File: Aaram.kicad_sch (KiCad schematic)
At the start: 51 parts, among them J1 Conn_01x03, J2 Conn_01x02, J3 AC_OUT, J4 SWITCH_IN, J5 5V_OUT, J6 PSU_AC_IN, J8 SPARE_PINS, K1 10A cube relay, K2 10A cube relay, K3 10A cube relay, Q1 BT136-600, Q2 2N2222A, Q3 2N2222A, Q4 2N2222A, U1 ESP32-DevKitC, U2 TLP281-4GB_F_

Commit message: Added 5v connection to relays
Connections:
- net +5V: now also D1.1 (K), D2.1 (K), D3.1 (K), K1.5, K2.5, K3.5
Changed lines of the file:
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@@
 	)
 	(junction
+		(at 236.22 121.92)
+		(diameter 0)
+		(color 0 0 0 0)
+	)
+	(junction
 		(at 184.15 95.25)
 		(diameter 0)
@@
 	)
 	(junction
+		(at 251.46 24.13)
+		(diameter 0)
+		(color 0 0 0 0)
+	)
+	(junction
 		(at 62.23 55.88)
 		(diameter 0)
@@
 	)
 	(junction
+		(at 240.03 71.12)
+		(diameter 0)
+		(color 0 0 0 0)
+	)
+	(junction
 		(at 72.39 25.4)
 		(diameter 0)
@@
 	)
 	(symbol
+		(lib_id "power:+5V")
+		(at 251.46 24.13 0)
+		(unit 1)
+		(exclude_from_sim no)
+		(in_bom yes)
+		(on_board yes)
+		(dnp no)
+		(property "Reference" "#PWR04"
+			(at 251.46 27.94 0)
+			(effects
+				(font
+					(size 1.27 1.27)
+				)
+				(hide yes)
+			)
+		)
+		(property "Value" "+5V"
+			(at 251.4601 20.32 90)
+			(effects
+				(font
+					(size 1.27 1.27)
+				)
+				(justify left)
+			)
+		)
+		(property "Footprint" ""
+			(at 251.46 24.13 0)
+			(effects
+				(font
+					(size 1.27 1.27)
+				)
+				(hide yes)
+			)
+		)
+		(property "Datasheet" ""
+			(at 251.46 24.13 0)
+			(effects
+				(font
+					(size 1.27 1.27)
+				)
+				(hide yes)
+			)
+		)
+		(property "Description" "Power symbol creates a global label with name \"+5V\""
+			(at 251.46 24.13 0)
+			(effects
+				(font
+					(size 1.27 1.27)
+				)
+				(hide yes)
+			)
+		)
+		(pin "1"
+		)
+		(instances
+			(project "Aaram"
+				(path "/29654a86-74fd-4059-9f21-82ff906cc333"
+					(reference "#PWR04")
+					(unit 1)
+				)
+			)
+		)
+	)
+	(symbol
 		(lib_id "PCM_Resistor_AKL:R_1206")
 		(at 62.23 44.45 180)
@@
 	)
 	(symbol
+		(lib_id "power:+5V")
+		(at 236.22 121.92 90)
+		(unit 1)
+		(exclude_from_sim no)
+		(in_bom yes)
+		(on_board yes)
+		(dnp no)
+		(property "Reference" "#PWR06"
+			(at 240.03 121.92 0)
+			(effects
+				(font
+					(size 1.27 1.27)
+				)
+				(hide yes)
+			)
+		)
+		(property "Value" "+5V"
+			(at 232.41 121.9199 90)
+			(effects
+				(font
+					(size 1.27 1.27)
+				)
+				(justify left)
+			)
+		)
+		(property "Footprint" ""
+			(at 236.22 121.92 0)
+			(effects
+				(font
+					(size 1.27 1.27)
+				)
+				(hide yes)
+			)
+		)
+		(property "Datasheet" ""
+			(at 236.22 121.92 0)
+			(effects
+				(font
+					(size 1.27 1.27)
+				)
+				(hide yes)
+			)
+		)
+		(property "Description" "Power symbol creates a global label with name \"+5V\""
+			(at 236.22 121.92 0)
+			(effects
+				(font
+					(size 1.27 1.27)
+				)
+				(hide yes)
+			)
+		)
+		(pin "1"
+		)
+		(instances
+			(project "Aaram"
+				(path "/29654a86-74fd-4059-9f21-82ff906cc333"
+					(reference "#PWR06")
+					(unit 1)
+				)
+			)
+		)
+	)
+	(symbol
 		(lib_id "PCM_Resistor_AKL:R_1206")
 		(at 165.1 127 0)
@@
 					(unit 1)
 				)
+			)
+		)
+	)
+	(symbol
+		(lib_id "power:+5V")
+		(at 240.03 71.12 90)
+		(unit 1)
+		(exclude_from_sim no)
+		(in_bom yes)
+		(on_board yes)
+		(dnp no)
+		(property "Reference" "#PWR05"
+			(at 243.84 71.12 0)
+			(effects
+				(font
+					(size 1.27 1.27)
+				)
+				(hide yes)
+			)
+		)
+		(property "Value" "+5V"
+			(at 236.22 71.1199 90)
+			(effects
+				(font
+					(size 1.27 1.27)
+				)
+				(justify left)
+			)
+		)
+		(property "Footprint" ""
+			(at 240.03 71.12 0)
+			(effects
+				(font
+					(size 1.27 1.27)
+				)
+				(hide yes)
+			)
+		)
+		(property "Datasheet" ""
+			(at 240.03 71.12 0)
+			(effects
+				(font
+					(size 1.27 1.27)
+				)
+				(hide yes)
+			)
+		)
+		(property "Description" "Power symbol creates a global label with name \"+5V\""
+			(at 240.03 71.12 0)
+			(effects
+				(font
+					(size 1.27 1.27)
+				)
+				(hide yes)
+			)
+		)
+		(pin "1"
+		)
+		(instances
+			(project "Aaram"
+				(path "/29654a86-74fd-4059-9f21-82ff906cc333"
+					(reference "#PWR05")
+					(unit 1)
+				)

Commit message: Updated Silkscreen and connections
Moved the fan control from GPIO4 to GPIO 13, made changes to the silkscreen and redid some of the tracks for better layout.
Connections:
- net SP1: no longer U1.15 (MTCK/GPIO13/ADC2_CH4)
- net T1_Pin: now also U1.15 (MTCK/GPIO13/ADC2_CH4); no longer U1.26 (ADC2_CH0/GPIO4)
- no-connect marks 18 -> 19
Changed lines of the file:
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@@
+	)
+	(no_connect
+		(at 106.68 97.79)
 	)
 	(no_connect
@@
 		)
 	)
+	(global_label "T1_Pin"
+		(shape input)
+		(at 40.64 100.33 180)
+		(fields_autoplaced yes)
+		(effects
+			(font
+				(size 1.27 1.27)
+			)
+			(justify right)
+		)
+		(property "Intersheetrefs" "${INTERSHEET_REFS}"
+			(at 31.4863 100.33 0)
+			(effects
+				(font
+					(size 1.27 1.27)
+				)
+				(justify right)
+				(hide yes)
+			)
+		)
+	)
 	(global_label "S1"
 		(shape input)
@@
 		)
 	)
-	(global_label "SP1"
-		(shape input)
-		(at 40.64 100.33 180)
-		(fields_autoplaced yes)
-		(effects
-			(font
-				(size 1.27 1.27)
-			)
-			(justify right)
-		)
-		(property "Intersheetrefs" "${INTERSHEET_REFS}"
-			(at 33.9658 100.33 0)
-			(effects
-				(font
-					(size 1.27 1.27)
-				)
-				(justify right)
-				(hide yes)
-			)
-		)
-	)
 	(global_label "S4"
 		(shape input)
@@
 				(hide yes)
 			)
-		)
-	)
-	(global_label "T1_Pin"
-		(shape input)
-		(at 106.68 97.79 0)
-		(fields_autoplaced yes)
-		(effects
-			(font
-				(size 1.27 1.27)
-			)
-			(justify left)
-		)
-		(property "Intersheetrefs" "${INTERSHEET_REFS}"
-			(at 115.8337 97.79 0)
-			(effects
-				(font
-					(size 1.27 1.27)
-				)
-				(justify left)
-				(hide yes)
-			)

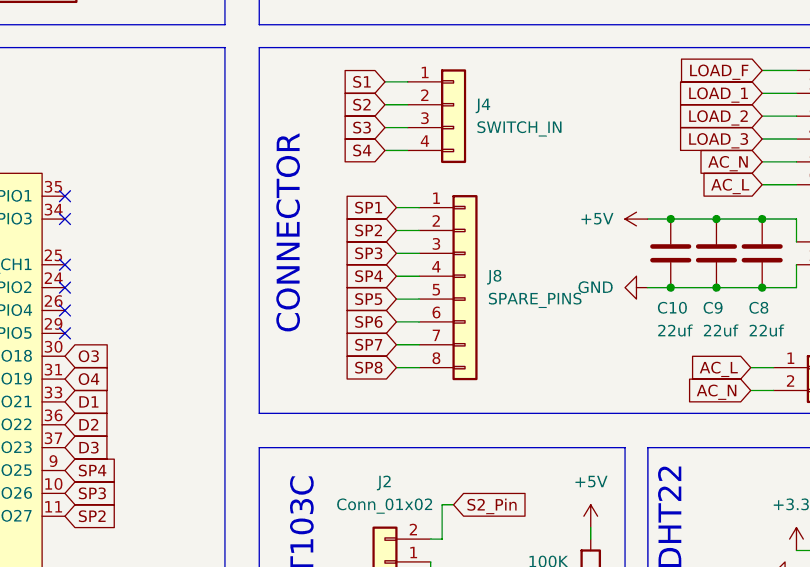
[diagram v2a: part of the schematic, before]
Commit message: Component update
Changed most of the components to use SMD form factor, updated clearance between components in the AC zone and updated the tracks.
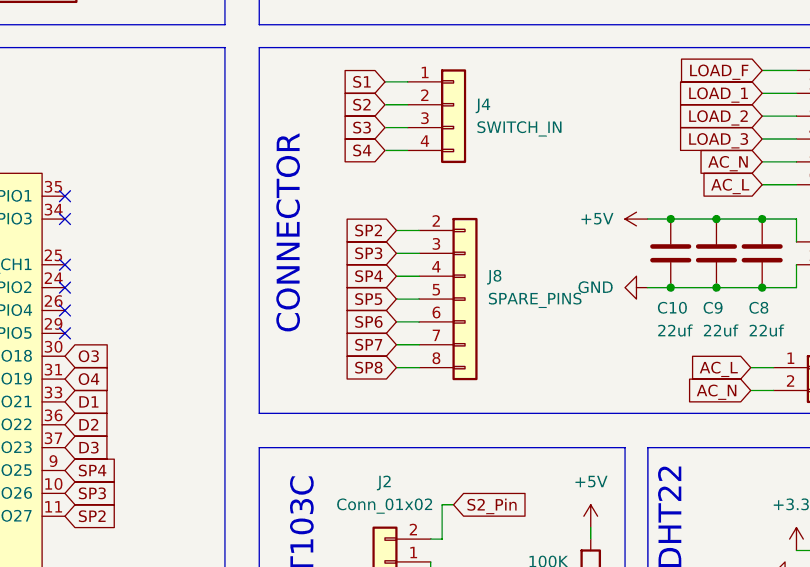
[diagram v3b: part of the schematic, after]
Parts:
- C10, C8, C9: footprint PCM_Capacitor_SMD_AKL:C_1206_3216Metric -> PCM_Capacitor_SMD_Handsoldering_AKL:C_1206_3216Metric_Pad1.42x1.75mm
- D1, D2, D3, D4, D5, D6, D7: footprint Diode_THT:D_DO-41_SOD81_P10.16mm_Horizontal -> Diode_SMD:D_SMA_Handsoldering
- Q2, Q3, Q4: footprint PCM_Package_TO_SOT_THT_AKL:TO-18-3_EBC -> PCM_Package_TO_SOT_SMD_AKL:SOT-23_BigPads
- R1, R10, R11, R12, R13, R14, R15, R16, R17, R2, R3, R4, R5, R6, R7, R8, R9: footprint PCM_Resistor_SMD_AKL:R_1206_3216Metric -> PCM_Capacitor_SMD_Handsoldering_AKL:C_1206_3216Metric_Pad1.42x1.75mm
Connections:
- removed net SP1: J8.1 (Pin_1)
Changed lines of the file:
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@@
 	(wire
 		(pts
-			(xy 143.51 86.36) (xy 146.05 86.36)
-		)
-		(stroke
-			(width 0)
-			(type default)
-		)
-	)
-	(wire
-		(pts
 			(xy 142.24 72.39) (xy 144.78 72.39)
 		)
@@
 		)
 	)
-	(global_label "SP1"
-		(shape input)
-		(at 143.51 86.36 180)
-		(fields_autoplaced yes)
-		(effects
-			(font
-				(size 1.27 1.27)
-			)
-			(justify right)
-		)
-		(property "Intersheetrefs" "${INTERSHEET_REFS}"
-			(at 136.8358 86.36 0)
-			(effects
-				(font
-					(size 1.27 1.27)
-				)
-				(justify right)
-				(hide yes)
-			)
-		)
-	)
 	(global_label "LOAD_F"
 		(shape input)
@@
 			)
 		)
-		(property "Footprint" "PCM_Package_TO_SOT_THT_AKL:TO-18-3_EBC"
+		(property "Footprint" "PCM_Package_TO_SOT_SMD_AKL:SOT-23_BigPads"
 			(at 254 91.44 0)
 			(effects
@@
 			)
 		)
-		(property "Footprint" "Diode_THT:D_DO-41_SOD81_P10.16mm_Horizontal"
+		(property "Footprint" "Diode_SMD:D_SMA_Handsoldering"
 			(at 68.58 20.955 0)
 			(effects
@@
 			)
 		)
-		(property "Footprint" "PCM_Resistor_SMD_AKL:R_1206_3216Metric"
+		(property "Footprint" "PCM_Capacitor_SMD_Handsoldering_AKL:C_1206_3216Metric_Pad1.42x1.75mm"
 			(at 62.23 33.02 0)
 			(effects
@@
 			)
 		)
-		(property "Footprint" "PCM_Resistor_SMD_AKL:R_1206_3216Metric"
+		(property "Footprint" "PCM_Capacitor_SMD_Handsoldering_AKL:C_1206_3216Metric_Pad1.42x1.75mm"
 			(at 226.06 46.99 0)
 			(effects
@@
 			)
 		)
-		(property "Footprint" "PCM_Resistor_SMD_AKL:R_1206_3216Metric"
+		(property "Footprint" "PCM_Capacitor_SMD_Handsoldering_AKL:C_1206_3216Metric_Pad1.42x1.75mm"
 			(at 190.5 24.13 0)
 			(effects
@@
 			)
 		)
-		(property "Footprint" "PCM_Resistor_SMD_AKL:R_1206_3216Metric"
+		(property "Footprint" "PCM_Capacitor_SMD_Handsoldering_AKL:C_1206_3216Metric_Pad1.42x1.75mm"
 			(at 33.02 40.64 0)
 			(effects
@@
 			)
 		)
-		(property "Footprint" "PCM_Capacitor_SMD_AKL:C_1206_3216Metric"
+		(property "Footprint" "PCM_Capacitor_SMD_Handsoldering_AKL:C_1206_3216Metric_Pad1.42x1.75mm"
 			(at 174.9552 95.25 0)
 			(effects
@@
 			)
 		)
-		(property "Footprint" "PCM_Resistor_SMD_AKL:R_1206_3216Metric"
+		(property "Footprint" "PCM_Capacitor_SMD_Handsoldering_AKL:C_1206_3216Metric_Pad1.42x1.75mm"
 			(at 33.02 10.16 0)
 			(effects
@@
 			)
 		)
-		(property "Footprint" "PCM_Package_TO_SOT_THT_AKL:TO-18-3_EBC"
+		(property "Footprint" "PCM_Package_TO_SOT_SMD_AKL:SOT-23_BigPads"
 			(at 254 44.45 0)
 			(effects
@@
 			)
 		)
-		(property "Footprint" "Diode_THT:D_DO-41_SOD81_P10.16mm_Horizontal"
+		(property "Footprint" "Diode_SMD:D_SMA_Handsoldering"
 			(at 68.58 43.815 0)
 			(effects
@@
 			)
 		)
-		(property "Footprint" "PCM_Resistor_SMD_AKL:R_1206_3216Metric"
+		(property "Footprint" "PCM_Capacitor_SMD_Handsoldering_AKL:C_1206_3216Metric_Pad1.42x1.75mm"
 			(at 165.1 148.59 0)
 			(effects
@@
 			)
 		)
-		(property "Footprint" "PCM_Capacitor_SMD_AKL:C_1206_3216Metric"
+		(property "Footprint" "PCM_Capacitor_SMD_Handsoldering_AKL:C_1206_3216Metric_Pad1.42x1.75mm"
 			(at 180.0352 95.25 0)
 			(effects
@@
 			)
 		)
-		(property "Footprint" "PCM_Resistor_SMD_AKL:R_1206_3216Metric"
+		(property "Footprint" "PCM_Capacitor_SMD_Handsoldering_AKL:C_1206_3216Metric_Pad1.42x1.75mm"
 			(at 62.23 10.16 0)
 			(effects
@@
 			)
 		)
-		(property "Footprint" "PCM_Resistor_SMD_AKL:R_1206_3216Metric"
+		(property "Footprint" "PCM_Capacitor_SMD_Handsoldering_AKL:C_1206_3216Metric_Pad1.42x1.75mm"
 			(at 166.37 36.83 0)
 			(effects
@@
 			)
 		)
-		(property "Footprint" "PCM_Resistor_SMD_AKL:R_1206_3216Metric"
+		(property "Footprint" "PCM_Capacitor_SMD_Handsoldering_AKL:C_1206_3216Metric_Pad1.42x1.75mm"
 			(at 62.23 17.78 0)
 			(effects
@@
 			)
 		)
-		(property "Footprint" "Diode_THT:D_DO-41_SOD81_P10.16mm_Horizontal"
+		(property "Footprint" "Diode_SMD:D_SMA_Handsoldering"
 			(at 235.585 31.75 0)
 			(effects
@@
 			)
 		)
-		(property "Footprint" "PCM_Resistor_SMD_AKL:R_1206_3216Metric"
+		(property "Footprint" "PCM_Capacitor_SMD_Handsoldering_AKL:C_1206_3216Metric_Pad1.42x1.75mm"
 			(at 154.94 36.83 0)
 			(effects
@@
 			)
 		)
-		(property "Footprint" "Diode_THT:D_DO-41_SOD81_P10.16mm_Horizontal"
+		(property "Footprint" "Diode_SMD:D_SMA_Handsoldering"
 			(at 231.775 129.54 0)
 			(effects
@@
 			)
 		)
-		(property "Footprint" "PCM_Resistor_SMD_AKL:R_1206_3216Metric"
+		(property "Footprint" "PCM_Capacitor_SMD_Handsoldering_AKL:C_1206_3216Metric_Pad1.42x1.75mm"
 			(at 33.02 33.02 0)
 			(effects
@@
 			)
 		)
-		(property "Footprint" "Diode_THT:D_DO-41_SOD81_P10.16mm_Horizontal"
+		(property "Footprint" "Diode_SMD:D_SMA_Handsoldering"
 			(at 39.37 43.815 0)
 			(effects
@@
 			)
 		)
-		(property "Footprint" "PCM_Package_TO_SOT_THT_AKL:TO-18-3_EBC"
+		(property "Footprint" "PCM_Package_TO_SOT_SMD_AKL:SOT-23_BigPads"
 			(at 250.19 142.24 0)
 			(effects
@@
 			)
 		)
-		(property "Footprint" "PCM_Resistor_SMD_AKL:R_1206_3216Metric"
+		(property "Footprint" "PCM_Capacitor_SMD_Handsoldering_AKL:C_1206_3216Metric_Pad1.42x1.75mm"
 			(at 62.23 40.64 0)
 			(effects
@@
 			)
 		)
-		(property "Footprint" "PCM_Resistor_SMD_AKL:R_1206_3216Metric"
+		(property "Footprint" "PCM_Capacitor_SMD_Handsoldering_AKL:C_1206_3216Metric_Pad1.42x1.75mm"
 			(at 222.25 144.78 0)
 			(effects
@@
 			)
 		)
-		(property "Footprint" "PCM_Resistor_SMD_AKL:R_1206_3216Metric"
+		(property "Footprint" "PCM_Capacitor_SMD_Handsoldering_AKL:C_1206_3216Metric_Pad1.42x1.75mm"
 			(at 165.1 138.43 0)
 			(effects
@@
 			)
 		)
-		(property "Footprint" "Diode_THT:D_DO-41_SOD81_P10.16mm_Horizontal"
+		(property "Footprint" "Diode_SMD:D_SMA_Handsoldering"
 			(at 39.37 20.955 0)
 			(effects
@@
 			)
 		)
-		(property "Footprint" "PCM_Resistor_SMD_AKL:R_1206_3216Metric"
+		(property "Footprint" "PCM_Capacitor_SMD_Handsoldering_AKL:C_1206_3216Metric_Pad1.42x1.75mm"
 			(at 157.48 36.83 0)
 			(effects
@@
 		(pin "6"
 		)
-		(pin "1"
-		)
 		(instances
 			(project ""
@@
 			)
 		)
-		(property "Footprint" "PCM_Capacitor_SMD_AKL:C_1206_3216Metric"
+		(property "Footprint" "PCM_Capacitor_SMD_Handsoldering_AKL:C_1206_3216Metric_Pad1.42x1.75mm"
 			(at 185.1152 95.25 0)
 			(effects
@@
 			)
 		)
-		(property "Footprint" "PCM_Resistor_SMD_AKL:R_1206_3216Metric"
+		(property "Footprint" "PCM_Capacitor_SMD_Handsoldering_AKL:C_1206_3216Metric_Pad1.42x1.75mm"
 			(at 226.06 93.98 0)
 			(effects
@@
 			)
 		)
-		(property "Footprint" "Diode_THT:D_DO-41_SOD81_P10.16mm_Horizontal"
+		(property "Footprint" "Diode_SMD:D_SMA_Handsoldering"
 			(at 235.585 78.74 0)
 			(effects
@@
 			)
 		)
-		(property "Footprint" "PCM_Resistor_SMD_AKL:R_1206_3216Metric"
+		(property "Footprint" "PCM_Capacitor_SMD_Handsoldering_AKL:C_1206_3216Metric_Pad1.42x1.75mm"
 			(at 33.02 17.78 0)
 			(effects

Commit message: Updated mostly everything
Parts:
- removed C10, C8, C9: 22uf, PCM_Capacitor_SMD_Handsoldering_AKL:C_1206_3216Metric_Pad1.42x1.75mm, symbol PCM_Capacitor_AKL:C_1206
- removed C3, C5, C6, C7: CP_Axial_L10.0mm_D4.5mm_P15.00mm, Xicor_Custom stuff:Axial_Capacitor_P10mm_W4.5mm, symbol PCM_Capacitor_AKL:CP_Axial_L10.0mm_D4.5mm_P15.00mm
- removed D4, D5, D6, D7: 1N4007, Diode_SMD:D_SMA_Handsoldering, symbol Diode:1N4007
- removed J8: SPARE_PINS, Connector_PinHeader_2.54mm:PinHeader_1x08_P2.54mm_Vertical, symbol Connector_Generic:Conn_01x08
- removed R11, R13: 10K, PCM_Capacitor_SMD_Handsoldering_AKL:C_1206_3216Metric_Pad1.42x1.75mm, symbol PCM_Resistor_AKL:R_1206
- removed R16: 1M, PCM_Capacitor_SMD_Handsoldering_AKL:C_1206_3216Metric_Pad1.42x1.75mm, symbol PCM_Resistor_AKL:R_1206
- removed U1: ESP32-DevKitC, Xicor_Custom stuff:ESP32_38Pin, symbol PCM_Espressif:ESP32-DevKitC
- removed U2: TLP281-4GB_F_, Xicor_Custom stuff:SOIC127P700X210-16N, symbol TLP281-4GB_F_:TLP281-4GB_F_
- added C11, C12, C6, C7: 10uf, PCM_Capacitor_SMD_Handsoldering_AKL:C_1206_3216Metric_Pad1.42x1.75mm, symbol PCM_Capacitor_AKL:C_Generic
- added C16: 1uf, PCM_Capacitor_SMD_Handsoldering_AKL:C_1206_3216Metric_Pad1.42x1.75mm, symbol PCM_Capacitor_AKL:C_Generic
- added C18, C19: 0.1uf, PCM_Capacitor_SMD_Handsoldering_AKL:C_1206_3216Metric_Pad1.42x1.75mm, symbol PCM_Capacitor_AKL:C_1206
- added D10, D11, D8, D9: MB6S, PCM_Diode_SMD_AKL:Diode_Bridge_MBS, symbol PCM_Diode_Bridge_AKL:MB6S
- added F1: Fuse, Xicor_Custom stuff:BLX-A, symbol PCM_Device_AKL:Fuse
- added J10, J11, J12, J13: Conn_01x03_Socket, Connector_JST:JST_SH_BM03B-SRSS-TB_1x03-1MP_P1.00mm_Vertical, symbol Connector_Generic:Conn_01x03
- added J7: Conn_01x05, Connector_PinHeader_2.54mm:PinHeader_1x05_P2.54mm_Vertical, symbol Connector_Generic:Conn_01x05
- added J8: USB_C_Receptacle_USB2.0_16P, Connector_USB:USB_C_Receptacle_GCT_USB4105-xx-A_16P_TopMnt_Horizontal, symbol Connector:USB_C_Receptacle_USB2.0_16P
- added J9: Conn_01x02, Connector_PinSocket_2.54mm:PinSocket_1x02_P2.54mm_Vertical, symbol Connector_Generic:Conn_01x02
- added R19, R23: 100K, PCM_Resistor_SMD_AKL:R_1206_3216Metric_Pad1.42x1.75mm_HandSolder, symbol PCM_Resistor_AKL:R_1206
- added R20, R25, R26, R27: 10K, PCM_Resistor_SMD_AKL:R_1206_3216Metric_Pad1.42x1.75mm_HandSolder, symbol PCM_Resistor_AKL:R_1206
- added R21, R22: 10k, PCM_Resistor_SMD_AKL:R_1206_3216Metric_Pad1.42x1.75mm_HandSolder, symbol PCM_Resistor_AKL:R_1206
- added RV1, RV2, RV3, RV4: Varistor, Xicor_Custom stuff:Varistor_10D431K, symbol Device:Varistor
- added SW1, SW4: SW_Push, Xicor_Custom stuff:Tactile switch 6x3, symbol Switch:SW_Push
- added SW2: SW_Push, Xicor_Custom stuff:SMD Tactile switch, symbol Switch:SW_Push
- added U1: ESP32-C6-MINI-1/U, PCM_Espressif:ESP32-C6-MINI-1, symbol PCM_Espressif:ESP32-C6-MINI-1/U
- added U2: AZ1117D-3.3TRE1, PCM_Package_TO_SOT_SMD_AKL:TO-252-2, symbol PCM_Voltage_Regulator_AKL:AZ1117D-3.3TRE1
- added U3: ~, Xicor_Custom stuff:Mini_Boost, symbol Xicor_Custom:Mini_Boost
- added U4: ~, Xicor_Custom stuff:TP4056-18650, symbol Xicor_Custom:TP4056-18650
- added U5: TLP281-4GB_F_, Xicor_Custom stuff:SOP127P780X200-16N, symbol TLP281-4GB_F_:TLP281-4GB_F_
- C1: symbol PCM_Capacitor_AKL:CP_Axial_L10.0mm_D4.5mm_P15.00mm -> PCM_Capacitor_AKL:C_3640
- C2: footprint Xicor_Custom stuff:Film_Cap_13x13mm_P5.00mm -> PCM_Capacitor_SMD_Handsoldering_AKL:C_1206_3216Metric_Pad1.42x1.75mm
- C4: symbol PCM_Capacitor_AKL:CP_Axial_L10.0mm_D4.5mm_P15.00mm -> PCM_Capacitor_US_AKL:C_0805
- J5: value 5V_OUT -> PSU_5V_OUT
- Q2, Q3, Q4: footprint PCM_Package_TO_SOT_SMD_AKL:SOT-23_BigPads -> PCM_Package_TO_SOT_THT_AKL:TO-18-3_EBC
- R1, R2, R3, R4, R5, R6, R7, R8, R9: footprint PCM_Capacitor_SMD_Handsoldering_AKL:C_1206_3216Metric_Pad1.42x1.75mm -> PCM_Resistor_SMD_AKL:R_1206_3216Metric_Pad1.42x1.75mm_HandSolder
- R10: value 1M -> 10k; footprint PCM_Capacitor_SMD_Handsoldering_AKL:C_1206_3216Metric_Pad1.42x1.75mm -> PCM_Resistor_SMD_AKL:R_1206_3216Metric_Pad1.42x1.75mm_HandSolder
- R12, R14: value 1M -> 5.1k; footprint PCM_Capacitor_SMD_Handsoldering_AKL:C_1206_3216Metric_Pad1.42x1.75mm -> PCM_Resistor_SMD_AKL:R_1206_3216Metric_Pad1.42x1.75mm_HandSolder
- R15, R17: value 10K -> 100K; footprint PCM_Capacitor_SMD_Handsoldering_AKL:C_1206_3216Metric_Pad1.42x1.75mm -> PCM_Resistor_SMD_AKL:R_1206_3216Metric_Pad1.42x1.75mm_HandSolder
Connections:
- net +3.3V: now also R10.1, C11.2, C12.2, J10.1 (Pin_1), J11.1 (Pin_1), J12.1 (Pin_1), J13.1 (Pin_1), R20.1, R21.2, R25.1, R26.1, R27.1, U1.3 (3V3), U2.2 (OUT)
- net +5V: now also C16.1, C6.2, C7.2, J8.A4 (VBUS), J8.A9 (VBUS), J8.B4 (VBUS), J8.B9 (VBUS), U2.3 (IN), U3.4 (+); no longer J5.1 (Pin_1)
- net AC_L: now also F1.1, RV1.2, RV2.2, RV3.2, RV4.1; no longer J3.6 (Pin_6)
- net AC_N: now also D10.4 (2), D11.4 (2), D8.4 (2), D9.4 (2); no longer R15.1, R17.1
- net D1: now also R2.2, U1.28 (GPIO22); no longer R3.2
- net D2: now also R1.2, U1.27 (GPIO21); no longer R2.2
- net D3: now also R3.2, U1.26 (GPIO20); no longer R1.2
- net GND: now also R12.1, R14.1, C11.1, C12.1, C16.2, C18.1, C19.1, C6.1, C7.1, J10.3 (Pin_3), J11.3 (Pin_3), J12.3 (Pin_3), J13.3 (Pin_3), J8.A1 (GND), J8.A12 (GND), J8.B1 (GND), J8.B12 (GND), J8.S1 (SHIELD), R22.1, SW1.1, SW4.1, U1.1 (GND), U1.11 (GND), U1.14 (GND), U1.2 (GND), U1.36 (GND), U1.37 (GND), U1.38 (GND), U1.39 (GND), U1.40 (GND), U1.41 (GND), U1.42 (GND), U1.43 (GND), U1.44 (GND), U1.45 (GND), U1.46 (GND), U1.47 (GND), U1.48 (GND), U1.49 (GND), U1.50 (GND), U1.51 (GND), U1.52 (GND), U1.53 (GND), U2.1, U3.3 (-), U4.2 (GND), U5.11 (ET3), U5.13 (ET2), U5.15 (ET1), U5.9 (ET4)
- net LOAD_1: now also J3.3 (Pin_3), RV3.1; no longer J3.2 (Pin_2)
- net LOAD_2: now also J3.2 (Pin_2), RV2.1; no longer J3.3 (Pin_3)
- net LOAD_3: now also RV1.1
- net LOAD_F: now also RV4.2
- net SP2: now also J7.2 (Pin_2), U1.5 (GPIO2/ADC1_CH2)
- net SP3: now also J7.3 (Pin_3), U1.6 (GPIO3/ADC1_CH3)
- net SP4: now also J7.4 (Pin_4), U1.9 (MTMS/GPIO4/ADC1_CH4)
- net SP5: now also J7.5 (Pin_5), U1.10 (MTDI/GPIO5/ADC1_CH5)
- net T1_Pin: now also U1.29 (GPIO23)
- net at D2.2 (A), K3.2: now also Q2.3 (C); no longer Q3.3 (C)
- net at R15.2: now also D9.1 (+); no longer R14.1
- net at R17.2: now also D10.1 (+)
- net at D3.2 (A), K2.2: now also Q3.3 (C); no longer Q4.3 (C)
- net at D1.2 (A), K1.2: now also Q4.3 (C); no longer Q2.3 (C)
- net S1: no longer names the net of R10.2
- net S1: now also C18.2, SW1.2, U1.8 (EN/CHIP_PU); no longer J4.1 (Pin_1)
- net S1_Pin renamed Sensor 1
- net Sensor 1: now also U1.15 (MTCK/GPIO6/ADC1_CH6)
- net S2: no longer names the net of R12.2
- net S2: now also J8.A5 (CC1); no longer J4.2 (Pin_2)
- net S2_Pin renamed Sensor 2
- net Sensor 2: now also U1.16 (MTDO/GPIO7)
- net S3 renamed AC_IN_3
- net AC_IN_3: now also D10.3 (1), J12.2 (Pin_2), R25.2, U1.24 (GPIO18), U5.12 (CT3)
- net S4: no longer names the net of R14.2
- net S4: now also J8.B5 (CC2); no longer J4.4 (Pin_4)
- new net: R19.1, U5.7 (A4)
- new net: D11.1 (+), R19.2
- new net: C19.2, R21.1, SW4.2, U1.22 (GPIO8)
- new net: SW2.1, U3.1 (+)
- new net: U3.2 (-), U4.4 (B_OUT-)
- new net: D8.1 (+), R23.2
- new net: F1.2, J3.6 (Pin_6)
- new net: R15.1, U5.3 (A2)
- new net: R23.1, U5.1 (A1)
- new net: R17.1, U5.5 (A3)
- new net: J9.1 (Pin_1), U4.5 (B_IN+)
- new net: J9.2 (Pin_2), U4.6 (B_IN-)
- new net: R22.2, U1.23 (GPIO9)
- new net: SW2.2, U4.3 (B_OUT+)
- new net AC_IN_1: D8.3 (1), J10.2 (Pin_2), J4.1 (Pin_1), R27.2, U1.19 (GPIO14), U5.16 (CT1)
- new net AC_IN_2: D9.3 (1), J11.2 (Pin_2), J4.2 (Pin_2), R26.2, U1.20 (GPIO15), U5.14 (CT2)
- new net AC_IN_4: D11.3 (1), J13.2 (Pin_2), J4.4 (Pin_4), R20.2, U1.25 (GPIO19), U5.10 (CT4)
- new net G1: D8.2 (-), U5.2 (C1)
- new net G2: D9.2 (-), U5.4 (C2)
- new net G3: D10.2 (-), U5.6 (C3)
- new net G4: D11.2 (-), U5.8 (C4)
- new net PSU_5V: J5.1 (Pin_1), U4.1 (5V)
- new net SP1: J7.1 (Pin_1), U1.13 (GPIO1/ADC1_CH1/XTAL_32K_N)
- new net USB+: J8.A6 (D+), J8.B6 (D+), U1.18 (GPIO13/USB_D+)
- new net USB-: J8.A7 (D-), J8.B7 (D-), U1.17 (GPIO12/USB_D-)
- no-connect marks 19 -> 6
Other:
- note added: "*Note Short Jumper A and B"
- note added: "5V out from PSU to TP4056"
- note added: "AC output header for loads"
- note added: "AC switch state detection"
- note added: "Battery"
- note added: "DHT_XX"
- note added: "DX and T1 are trigger pins for relay and triac"
- note added: "ESP32_C6_MINI"
- note added: "I'm taking the output from the switch board switches that already have Live connected and rectifying them for the TLP281 opto to give a digital signal the ESP"
- note added: "Input from switch board switches"
- note added: "PSU input headers"
- note added: "SENSORS"
- note added: "SP are spare pins"
- note added: "Spare ESP pins"
- note added: "TTP223"
- note added: "USB"
- note added: "VRM"
- note added: "ZMCT103C"
- note removed: "CONNECTOR"
- note removed: "ESP32_38PIN_CONN"
- note removed: "OPTO_STUFF"
- note removed: "SENSOR_DHT22"
- note removed: "SENSOR_ZMCT103C"
- moved on the sheet: C2, D1, D2, D3, J1, K1, K2, K3, R8, R9
